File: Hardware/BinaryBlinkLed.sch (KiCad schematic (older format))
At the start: 14 parts, among them IC1 ATTINY13A-SS, P1 SWITCH, P2 ISCP6, Q1 BC848, Q2 BC848

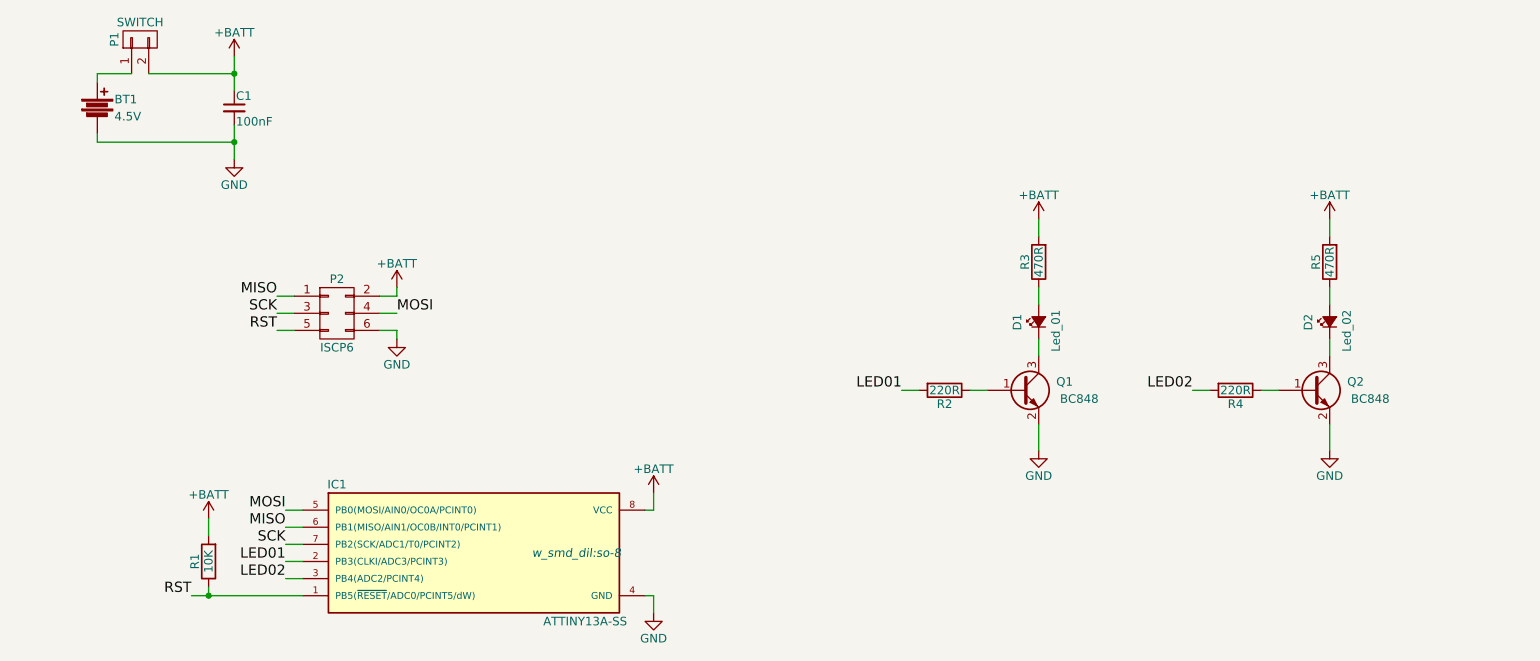
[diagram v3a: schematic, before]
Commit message: update of schematic, change footprint of switch and battery
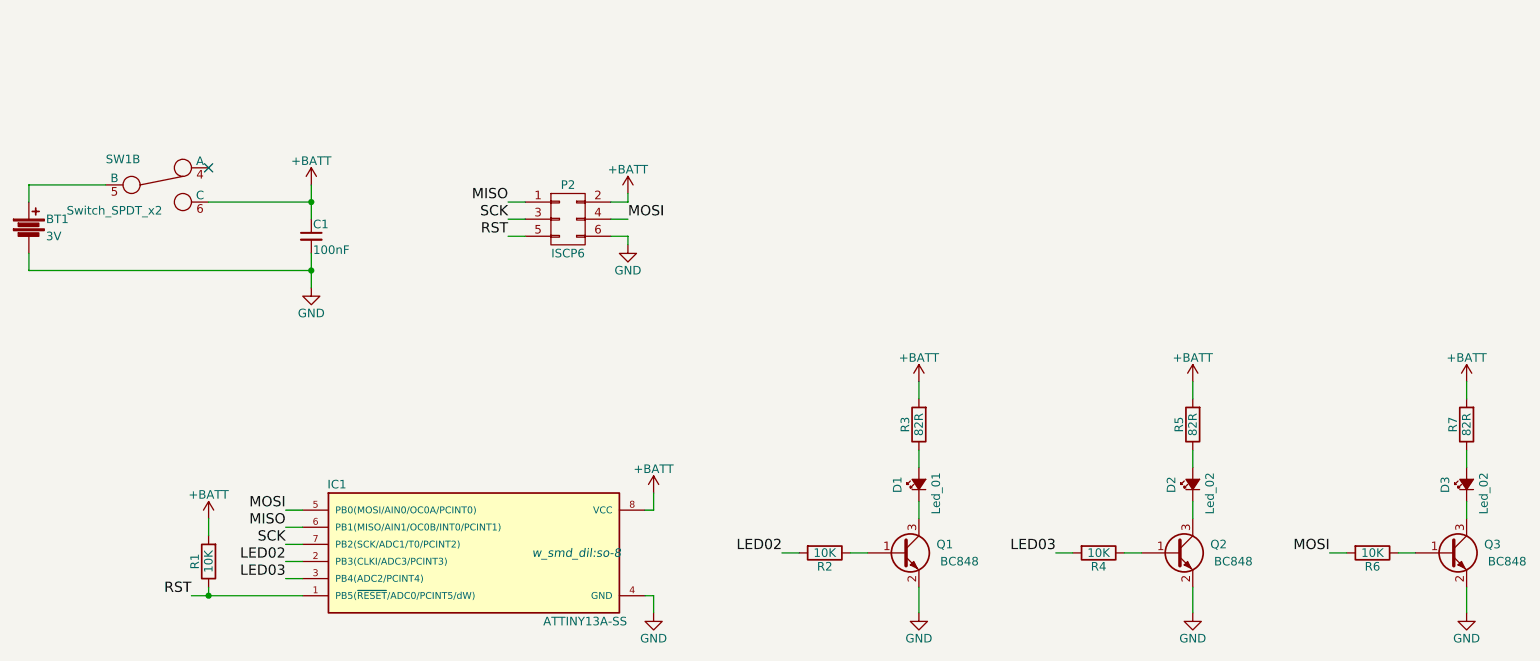
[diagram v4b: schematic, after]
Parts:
- removed P1: SWITCH, w_switch:switch_mmp122-r, symbol CONN_01X02
- added D3: Led_02, w_smd_leds:Led_1206, symbol Led_Small
- added Q3: BC848, TO_SOT_Packages_SMD:SOT-23, symbol Q_NPN_BEC
- added R6: 10K, Resistors_SMD:R_0805, symbol R
- added R7: 82R, Resistors_SMD:R_0805, symbol R
- added SW1: Switch_SPDT_x2, mc_switch:push_lock_6mm, symbol Switch_SPDT_x2
- BT1: value 4.5V -> 3V; footprint Connect:bornier2 -> JG_Misc:JG_BAT
- R2, R4: value 220R -> 10K
- R3, R5: value 470R -> 82R
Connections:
- net LED01 is gone; now on net LED02: IC1.2 (PB3(CLKI/ADC3/PCINT3)), R2.2
- net +BATT: now also R7.2, SW1.6 (C)
- net GND: now also Q3.2 (E)
- net LED02: no longer IC1.3 (PB4(ADC2/PCINT4)), R4.2
- net MOSI: now also R6.2
- net at BT1.1: now also SW1.5 (B)
- new net: Q3.1 (B), R6.1
- new net: D3.1 (K), Q3.3 (C)
- new net: D3.2 (A), R7.1
- new net LED03: IC1.3 (PB4(ADC2/PCINT4)), R4.2
- no-connect marks 0 -> 1
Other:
- moved on the sheet: BT1, C1, D1, D2, P2, Q1, Q2, R2, R3, R4, R5

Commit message: footprinft resistor changed, walter library used
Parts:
- R1, R2, R3, R4, R5, R6, R7: footprint Resistors_SMD:R_0805 -> w_smd_resistors:r_0805
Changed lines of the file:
@@
 F 0 "R2" V 5730 4500 50  0000 C CNN
 F 1 "10K" V 5650 4500 50  0000 C CNN
-F 2 "Resistors_SMD:R_0805" V 5580 4500 50  0001 C CNN
+F 2 "w_smd_resistors:r_0805" V 5580 4500 50  0001 C CNN
 F 3 "" H 5650 4500 50  0000 C CNN
 	1    5650 4500
@@
 F 0 "R3" V 6280 3750 50  0000 C CNN
 F 1 "82R" V 6200 3750 50  0000 C CNN
-F 2 "Resistors_SMD:R_0805" V 6130 3750 50  0001 C CNN
+F 2 "w_smd_resistors:r_0805" V 6130 3750 50  0001 C CNN
 F 3 "" H 6200 3750 50  0000 C CNN
 	1    6200 3750
@@
 F 0 "R4" V 7330 4500 50  0000 C CNN
 F 1 "10K" V 7250 4500 50  0000 C CNN
-F 2 "Resistors_SMD:R_0805" V 7180 4500 50  0001 C CNN
+F 2 "w_smd_resistors:r_0805" V 7180 4500 50  0001 C CNN
 F 3 "" H 7250 4500 50  0000 C CNN
 	1    7250 4500
@@
 F 0 "R5" V 7880 3750 50  0000 C CNN
 F 1 "82R" V 7800 3750 50  0000 C CNN
-F 2 "Resistors_SMD:R_0805" V 7730 3750 50  0001 C CNN
+F 2 "w_smd_resistors:r_0805" V 7730 3750 50  0001 C CNN
 F 3 "" H 7800 3750 50  0000 C CNN
 	1    7800 3750
@@
 F 0 "R1" V 2130 4550 50  0000 C CNN
 F 1 "10K" V 2050 4550 50  0000 C CNN
-F 2 "Resistors_SMD:R_0805" V 1980 4550 50  0001 C CNN
+F 2 "w_smd_resistors:r_0805" V 1980 4550 50  0001 C CNN
 F 3 "" H 2050 4550 50  0000 C CNN
 	1    2050 4550
@@
 F 0 "R6" V 8930 4500 50  0000 C CNN
 F 1 "10K" V 8850 4500 50  0000 C CNN
-F 2 "Resistors_SMD:R_0805" V 8780 4500 50  0001 C CNN
+F 2 "w_smd_resistors:r_0805" V 8780 4500 50  0001 C CNN
 F 3 "" H 8850 4500 50  0000 C CNN
 	1    8850 4500
@@
 F 0 "R7" V 9480 3750 50  0000 C CNN
 F 1 "82R" V 9400 3750 50  0000 C CNN
-F 2 "Resistors_SMD:R_0805" V 9330 3750 50  0001 C CNN
+F 2 "w_smd_resistors:r_0805" V 9330 3750 50  0001 C CNN
 F 3 "" H 9400 3750 50  0000 C CNN
 	1    9400 3750
